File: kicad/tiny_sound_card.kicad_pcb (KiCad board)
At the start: 2 copper layers, 91 x 55 mm, 49 parts, among them CON1 BARREL_JACK, IC1 ATMEGA328P-A, J1 TRS_JACK, M1 DFR0299, P1 EXT_PWR, P10 M3Drill, P2 SPKOUT, P3 EXT_SW0, P4 EXT_I2C, P4 M3Drill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

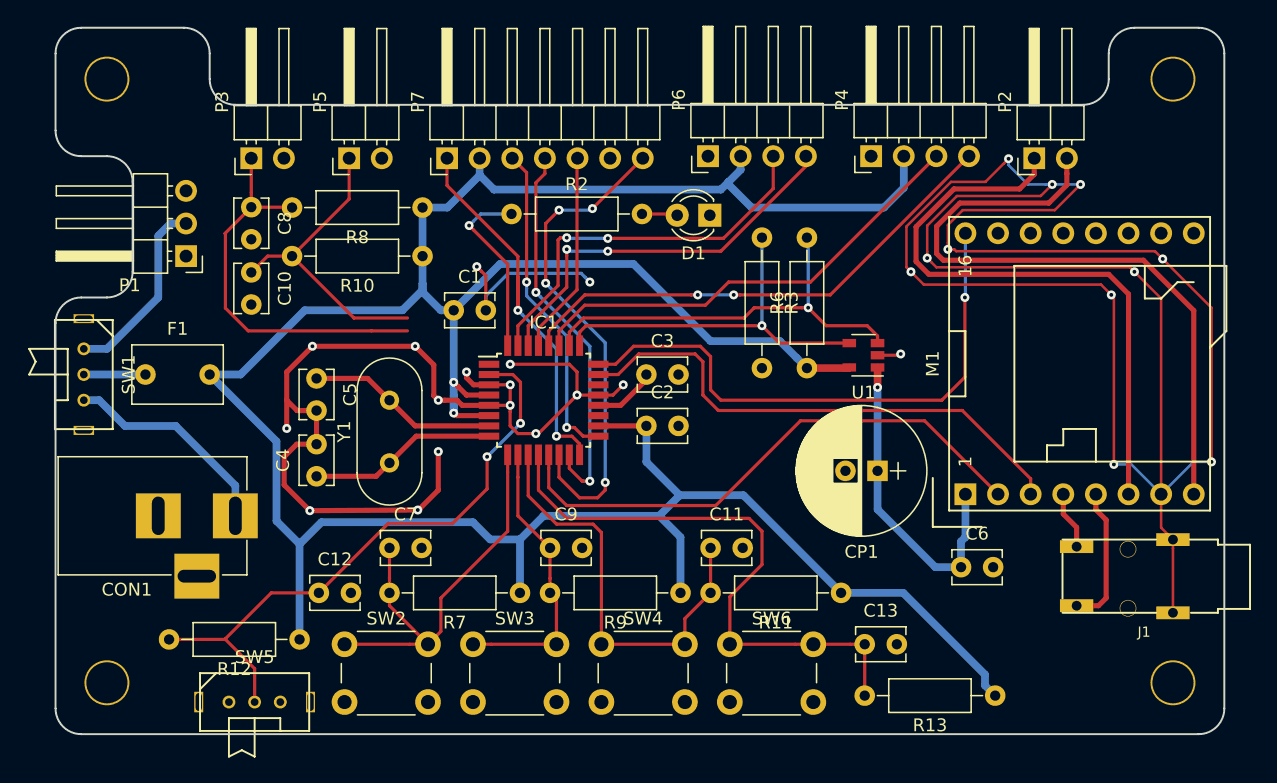
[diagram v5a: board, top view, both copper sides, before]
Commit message: EXT_SW1を削除
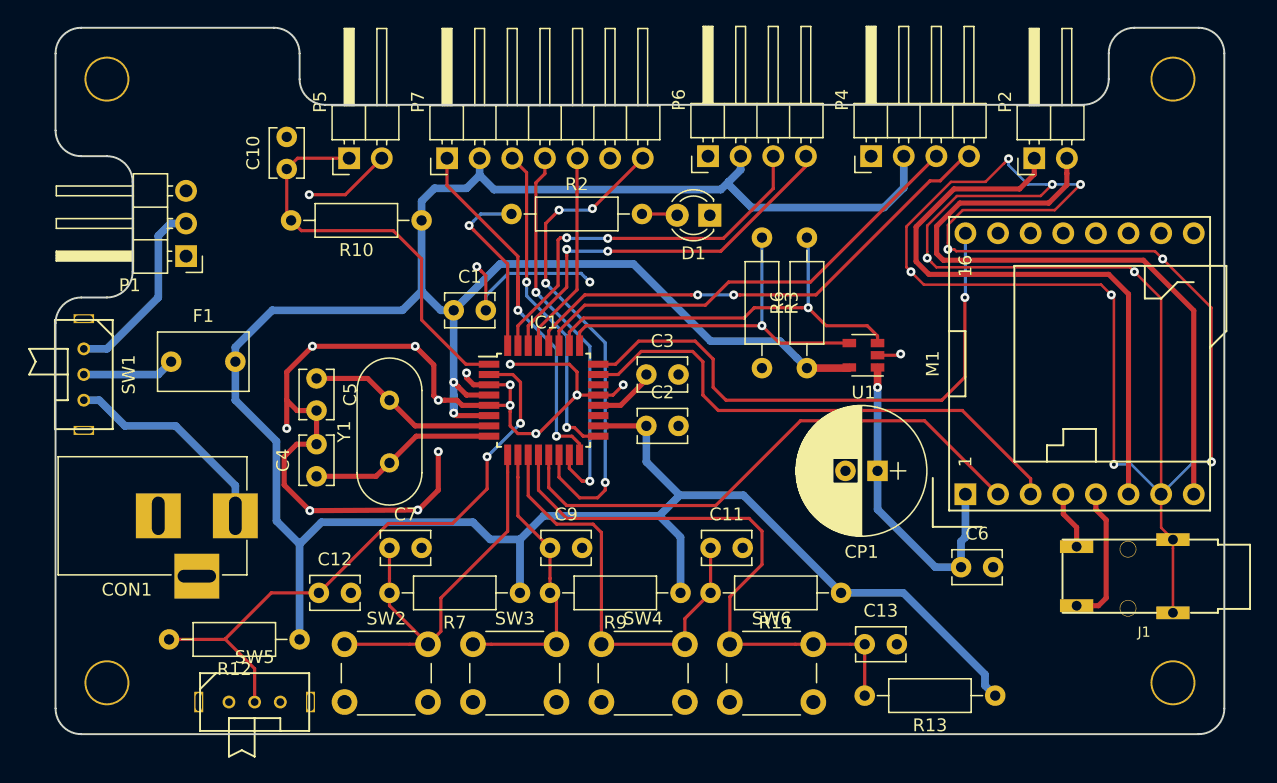
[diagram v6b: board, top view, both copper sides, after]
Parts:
- removed C8: 0.1u, Capacitors_ThroughHole:C_Disc_D3.8mm_W2.6mm_P2.50mm
- removed P3: EXT_SW0, Pin_Headers:Pin_Header_Angled_1x02_Pitch2.54mm
- removed R8: 47k, Resistors_ThroughHole:R_Axial_DIN0207_L6.3mm_D2.5mm_P10.16mm_Horizontal
- P5: value EXT_SW1 -> EXT_SW0
- moved C10 8.51 mm to (69.0, 72.0), turned to 90 degrees
- moved R10 2.78 mm to (79.5, 76.0)
- moved F1 2.24 mm to (60.0, 87.0)
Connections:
- C10 pad 1: /EXT_SW1 -> /D3
- P5 pad 1: /EXT_SW1 -> /D3
- R10 pad 2: /EXT_SW1 -> /D3
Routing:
- net /D3: track 0.00 -> 32.2 mm
- net /EXT_SW0: track 30.6 -> 0.00 mm
- net /EXT_SW1: track 24.1 -> 0.00 mm
- net GND: track 259.4 -> 266.2 mm, vias 28 -> 29
- net /SEL_VCC: track 4.80 -> 7.21 mm
- net VCC: track 235.8 -> 234.0 mm
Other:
- outline, holes or cut-outs redrawn

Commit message: ベタ配線
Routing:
- net GND: track 266.2 -> 674.7 mm, vias 29 -> 190
- net VCC: track 234.0 -> 239.8 mm, vias 2 -> 7
- net /D3: track 32.2 -> 29.4 mm
- net /D10: track 38.6 -> 35.9 mm
- net /D1: track 30.5 -> 32.2 mm
- net /CONN_VCC: track 16.9 -> 18.5 mm
- net /DFR_VCC: track 25.2 -> 26.7 mm
- net /ATMEGA_TX: track 43.2 -> 44.5 mm
- net /D0: track 31.2 -> 32.4 mm
- net /D11: track 30.2 -> 29.5 mm
- added copper zone on B.Cu, net GND
- added copper zone on F.Cu, net GND
